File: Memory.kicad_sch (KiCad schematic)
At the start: 6 parts, among them U8 74CBTLV3257_VQFN, U9 W25Q80DV_SOIC-8

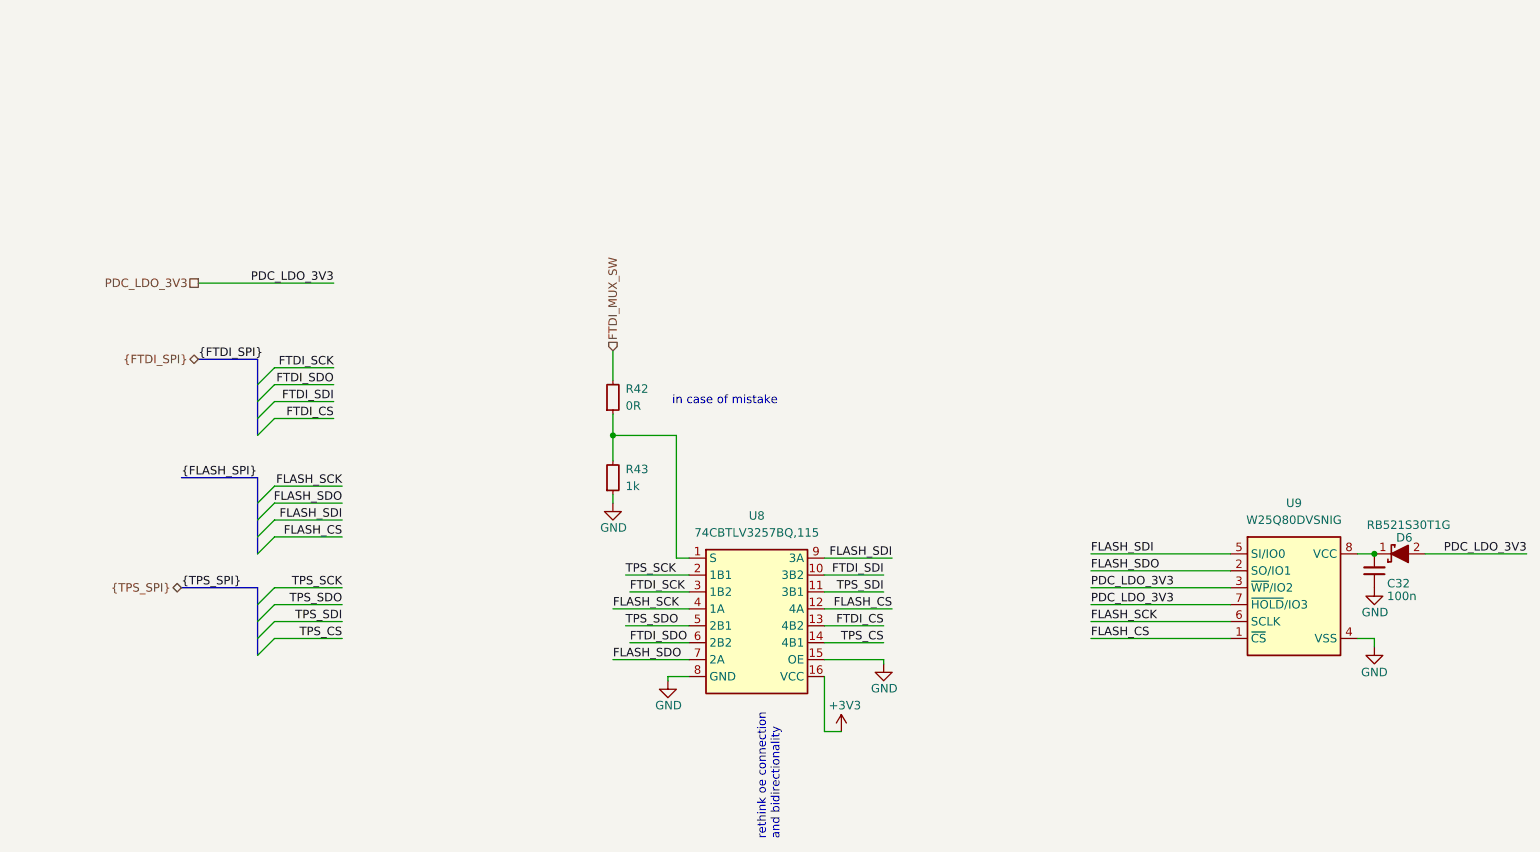
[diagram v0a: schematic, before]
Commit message: [#62623] Improve schematic, change 3V3 buck inductor, correct SPI, add testpoint
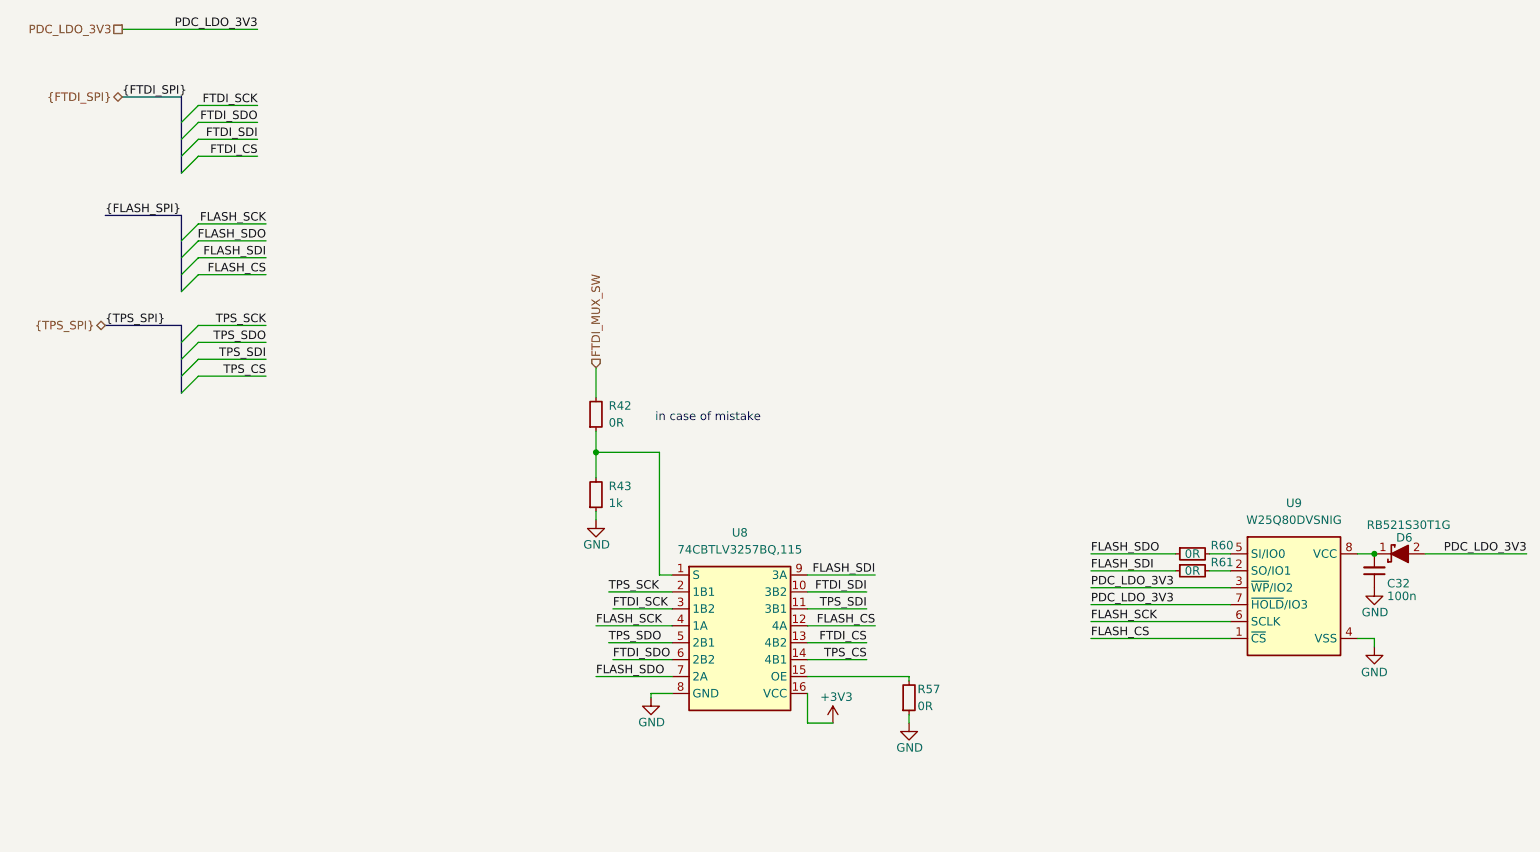
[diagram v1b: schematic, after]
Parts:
- added R57, R60, R61: R_0R_0402, antmicro-footprints:R_0402_1005Metric, symbol antmicroResistors0402:R_0R_0402
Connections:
- net FLASH_SDI: now also R61.1; no longer U9.5 (SI/IO0)
- net FLASH_SDO: now also R60.1; no longer U9.2 (SO/IO1)
- net GND: now also R57.1; no longer U8.15 (OE)
- new net: R57.2, U8.15 (OE)
- new net: R60.2, U9.5 (SI/IO0)
- new net: R61.2, U9.2 (SO/IO1)
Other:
- note removed: "rethink oe connection and bidirectionality"
- moved on the sheet: R42, R43, U8

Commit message: [#62623] Change hierarchy implementation
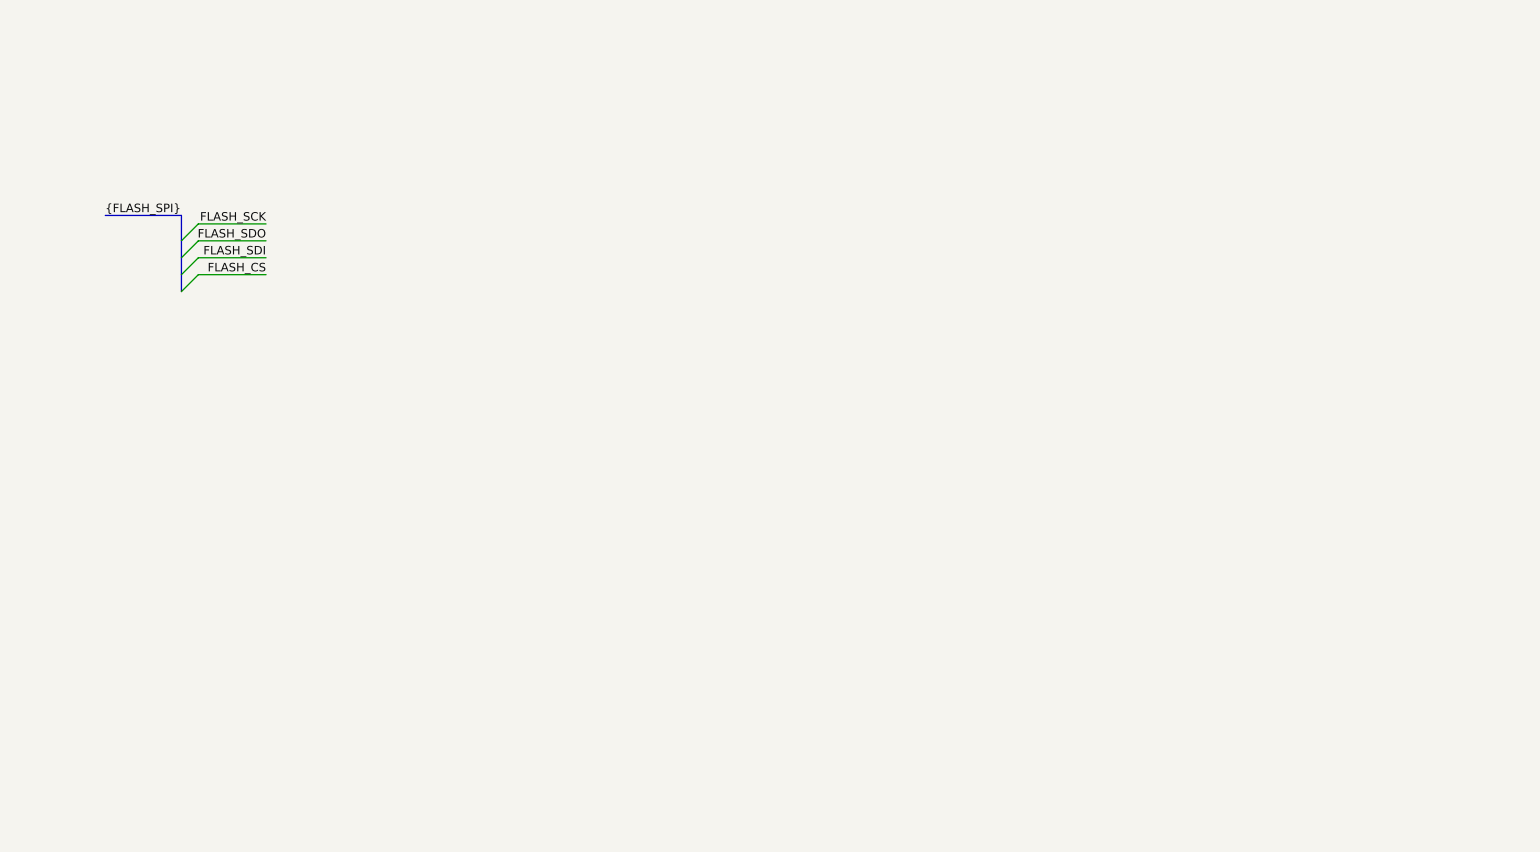
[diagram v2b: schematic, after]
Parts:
- removed C32: C_100n_0402, antmicro-footprints:C_0402_1005Metric, symbol antmicroCapacitors0402:C_100n_0402
- removed D6: RB521S30T1G, antmicro-footprints:SOD-523, symbol antmicroDiodesRectifiersSingle:RB521S30T1G
- removed R42, R57, R60, R61: R_0R_0402, antmicro-footprints:R_0402_1005Metric, symbol antmicroResistors0402:R_0R_0402
- removed R43: R_1k_0402, antmicro-footprints:R_0402_1005Metric, symbol antmicroResistors0402:R_1k_0402
- removed U8: 74CBTLV3257_VQFN, antmicro-footprints:DHVQFN-16-1EP_2.5x3.5mm_P0.5mm, symbol antmicroInterfaceAnalogSwitchesMultiplexersDemultiplexers:74CBTLV3257_VQFN
- removed U9: W25Q80DV_SOIC-8, antmicro-footprints:SOIC-8_3.9x4.9x1.75mm_P1.27mm, symbol antmicroMemory:W25Q80DV_SOIC-8
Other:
- note removed: "in case of mistake"
